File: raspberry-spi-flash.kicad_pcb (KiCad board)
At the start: 2 copper layers, 85 x 56 mm, 32 parts, among them J1 RJ45, P1 CONN_13X2, Q1 BSS138, SW1 SW_SPDT, SW2 SW_SPDT, U1 MX25L25735, U2 AT25SF081-SSHD-X, U3 MAX3232, U4 TXB0104D, U5 MIC5355-SGYMME

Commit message: Fixed typo
Signed-off-by: Aaron Williams <aaron.w2@gmail.com>
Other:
- board text added: "Disable to install or remove Flash!"
- board text removed: "Disable to install or remove Flast!"
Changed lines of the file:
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@@
   )
   (setup
-    (last_trace_width 1)
+    (last_trace_width 0.2)
     (user_trace_width 0.2)
     (user_trace_width 0.25)
@@
   (gr_line (start 189.3 170.675) (end 189.575 170.4) (layer F.SilkS) (width 0.3))
   (gr_line (start 186 170.675) (end 189.3 170.675) (layer F.SilkS) (width 0.3))
-  (gr_text "Disable to install\nor remove\nFlast!" (at 196.625 151.225) (layer F.SilkS)
+  (gr_text "Disable to install\nor remove\nFlash!" (at 196.625 151.225) (layer F.SilkS)
     (effects (font (size 1.5 1.5) (thickness 0.3)))
   )

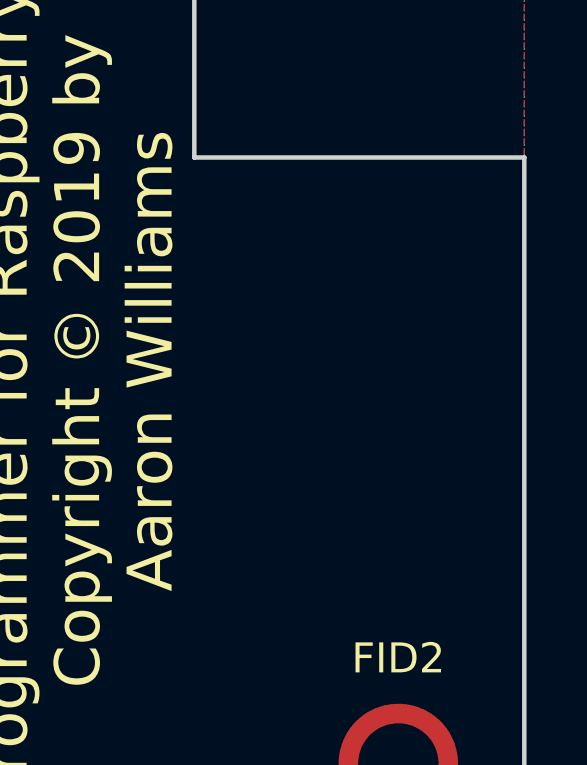
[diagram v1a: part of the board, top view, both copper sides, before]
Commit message: Fixed solder mask clearance.
Signed-off-by: Aaron Williams <aaron.w2@gmail.com>
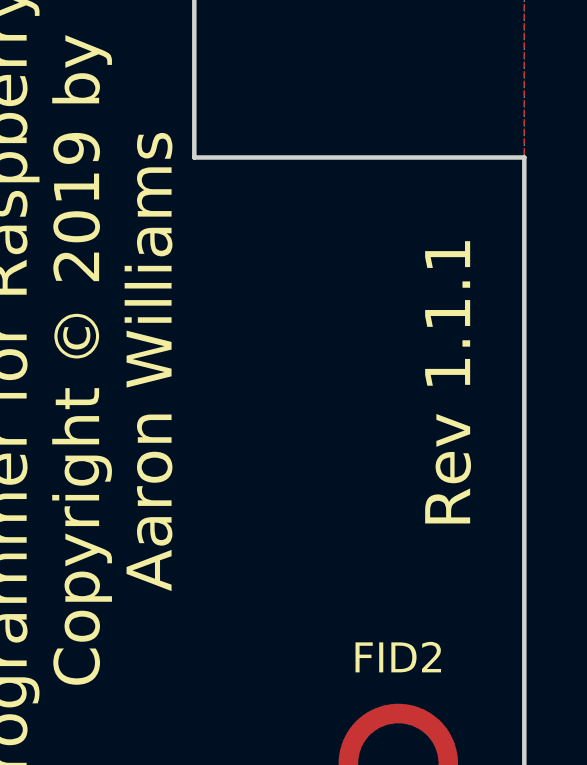
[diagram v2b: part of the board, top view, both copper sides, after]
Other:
- rule pad_to_mask_clearance: 0 -> -0.0508
- board text added: "Rev 1.1.1"
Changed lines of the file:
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@@
   (general
     (thickness 1.6)
-    (drawings 47)
+    (drawings 48)
     (tracks 387)
     (zones 0)
@@
   (title_block
     (title "Raspberry Pi SOIC-16 SPI Flash Programmer")
-    (date 2019-01-12)
-    (rev 1.1)
+    (date 2019-01-25)
+    (rev 1.1.1)
   )
   (layers
@@
     (pad_size 1 1)
     (pad_drill 0.6)
-    (pad_to_mask_clearance 0)
+    (pad_to_mask_clearance -0.0508)
     (solder_mask_min_width 0.25)
     (aux_axis_origin 143.5 181)
@@
     )
   )
+  (gr_text "Rev 1.1.1" (at 226 164.5 90) (layer F.SilkS)
+    (effects (font (size 1.5 1.5) (thickness 0.3)))
+  )
   (gr_line (start 189.3 170.675) (end 189.575 170.4) (layer F.SilkS) (width 0.3))

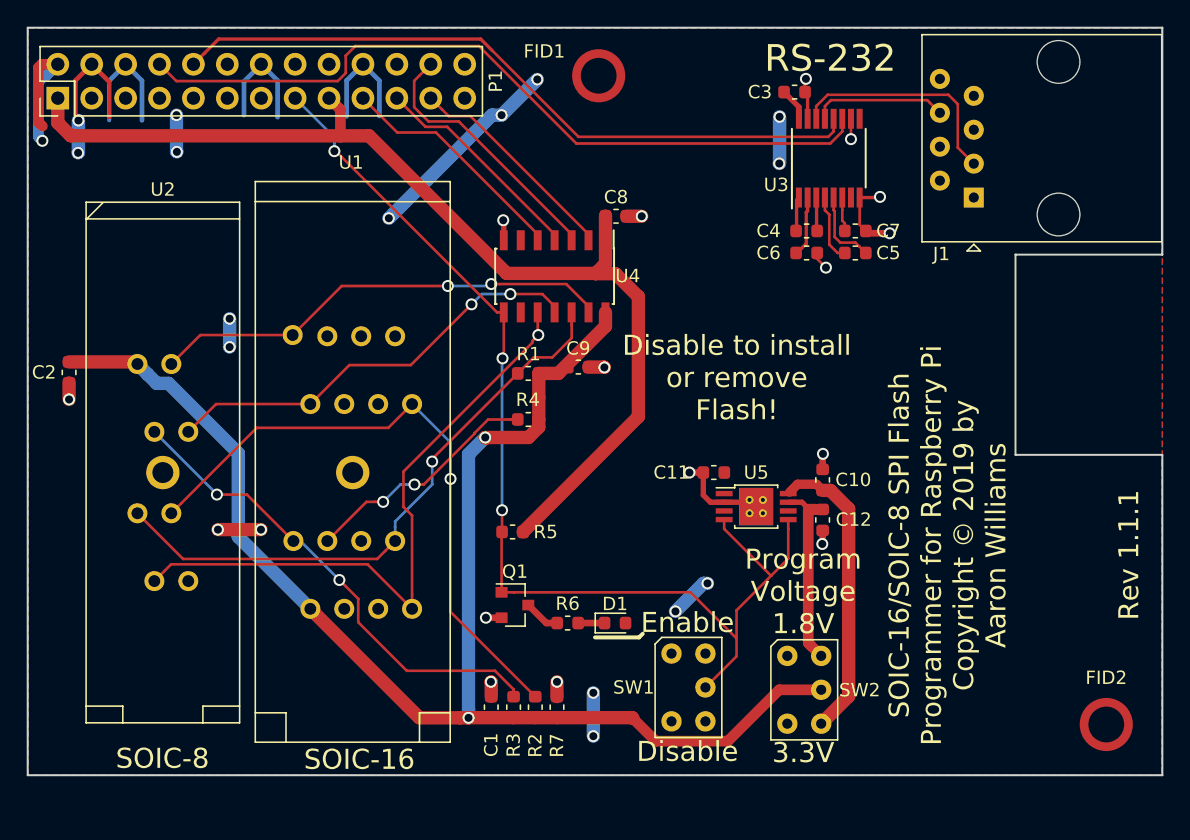
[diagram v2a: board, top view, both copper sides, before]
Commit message: Fixed footprint for soic-16 socket.
Signed-off-by: Aaron Williams <aaron.w2@gmail.com>
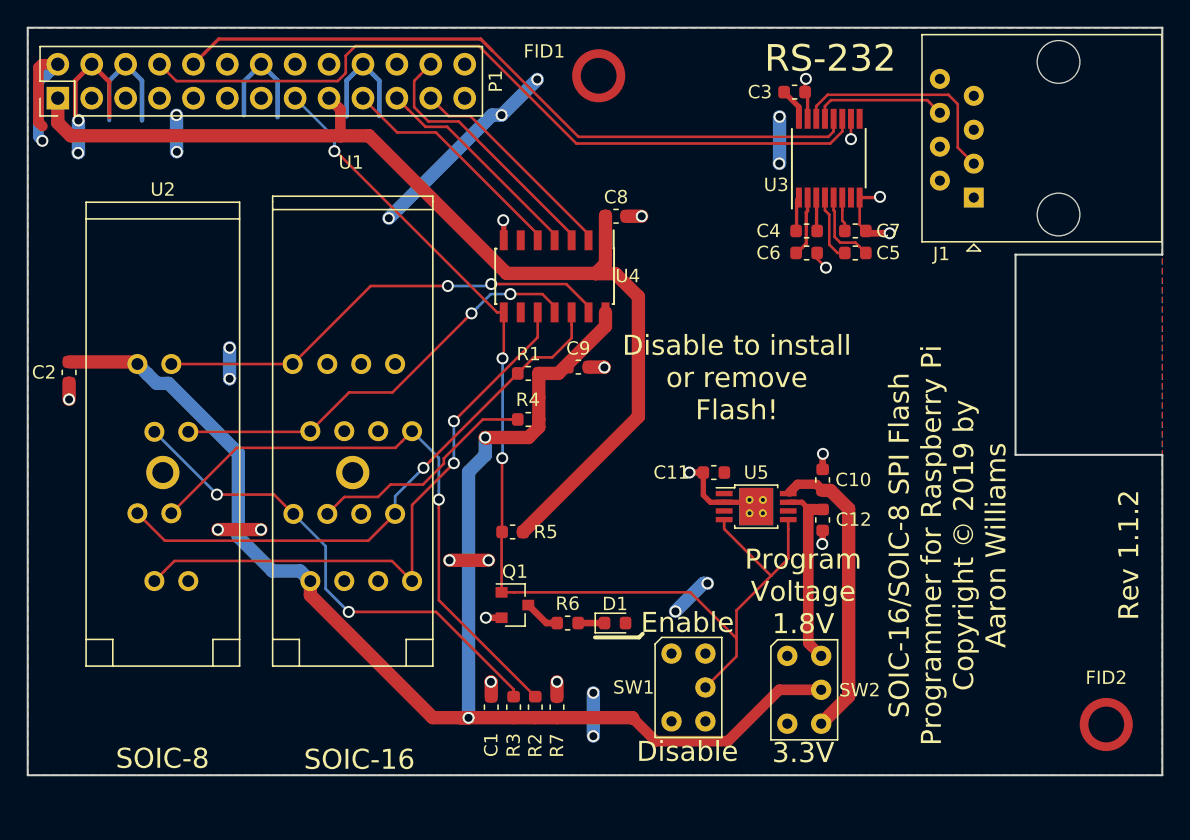
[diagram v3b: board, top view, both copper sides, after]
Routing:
- net /MISO: track 47.9 -> 44.6 mm, vias 1 -> 2
- net GND: track 60.2 -> 63.1 mm, vias 17 -> 19
- net Net-(R2-Pad2): track 47.2 -> 44.3 mm
- net /FL_CS0: track 44.7 -> 42.4 mm
- net VPP: track 110.9 -> 112.1 mm
- net Net-(R3-Pad2): track 36.5 -> 37.3 mm
- net Net-(R4-Pad2): track 18.6 -> 18.0 mm, vias 2 -> 0
- net Net-(U1-Pad4): track 0.00 -> 0.64 mm
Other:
- board text added: "Rev 1.1.2"
- board text removed: "Rev 1.1.1"
